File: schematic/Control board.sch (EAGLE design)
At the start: 14 parts, among them IC2 ATTINY44A

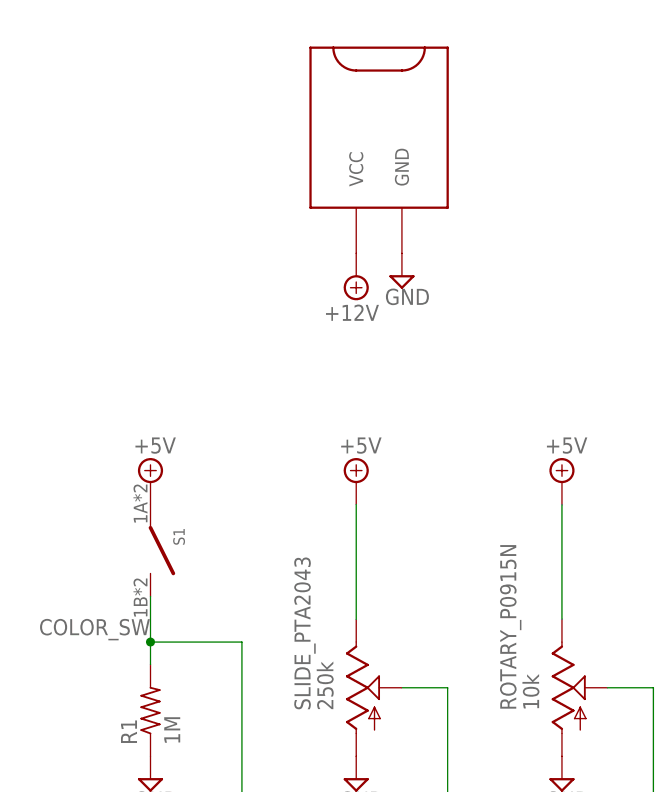
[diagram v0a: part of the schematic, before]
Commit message: Made the board a bit smaller, but there's still room to shrink it more
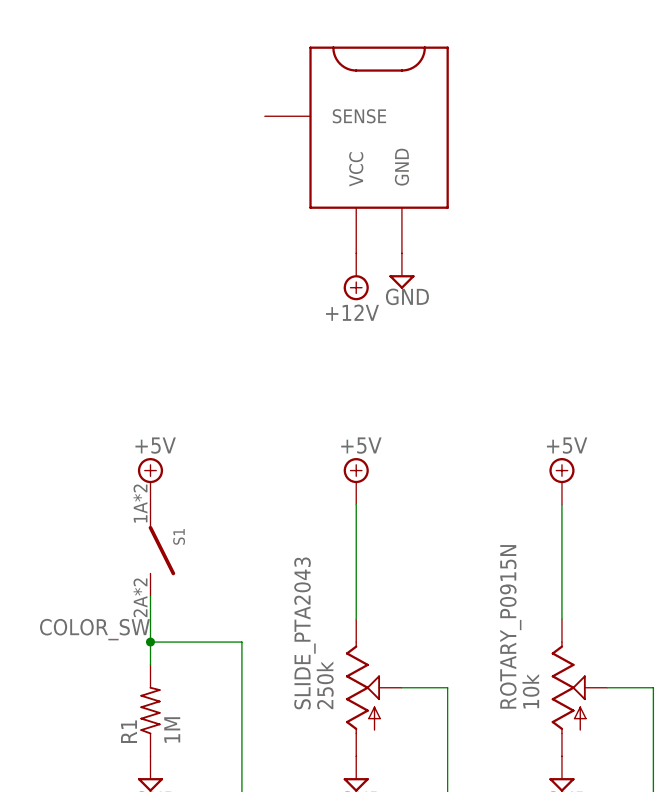
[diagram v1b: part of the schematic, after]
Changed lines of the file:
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@@
-</segment>
-<segment>
-<pinref part="POW1" gate="G$1" pin="GND"/>
-<pinref part="SUPPLY10" gate="GND" pin="GND"/>
 </segment>
 <segment>
@@
 <pinref part="CONN1" gate="G$1" pin="P$1"/>
 </segment>
+<segment>
+<pinref part="POW1" gate="G$1" pin="GND"/>
+<pinref part="SUPPLY10" gate="GND" pin="GND"/>
+</segment>
 </net>
 <net name="+12V" class="0">
@@
 </segment>
 <segment>
-<pinref part="POW1" gate="G$1" pin="VCC"/>
-<pinref part="SUPPLY9" gate="+12V" pin="+12V"/>
-</segment>
-<segment>
 <pinref part="SUPPLY16" gate="+12V" pin="+12V"/>
 <pinref part="CONN1" gate="G$1" pin="P$4"/>
 <wire x1="-27.94" y1="-71.12" x2="-30.48" y2="-71.12" width="0.1524" layer="91"/>
 </segment>
+<segment>
+<pinref part="POW1" gate="G$1" pin="VCC"/>
+<pinref part="SUPPLY9" gate="+12V" pin="+12V"/>
+</segment>
 </net>
